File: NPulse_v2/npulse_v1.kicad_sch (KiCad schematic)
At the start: 20 parts, among them J3 Conn_01x04_Pin, J4 USB_B_Micro, SW3 SW_Push, SW4 SW_SPDT, U2 STM32F103C8T6, Y2 16MHz

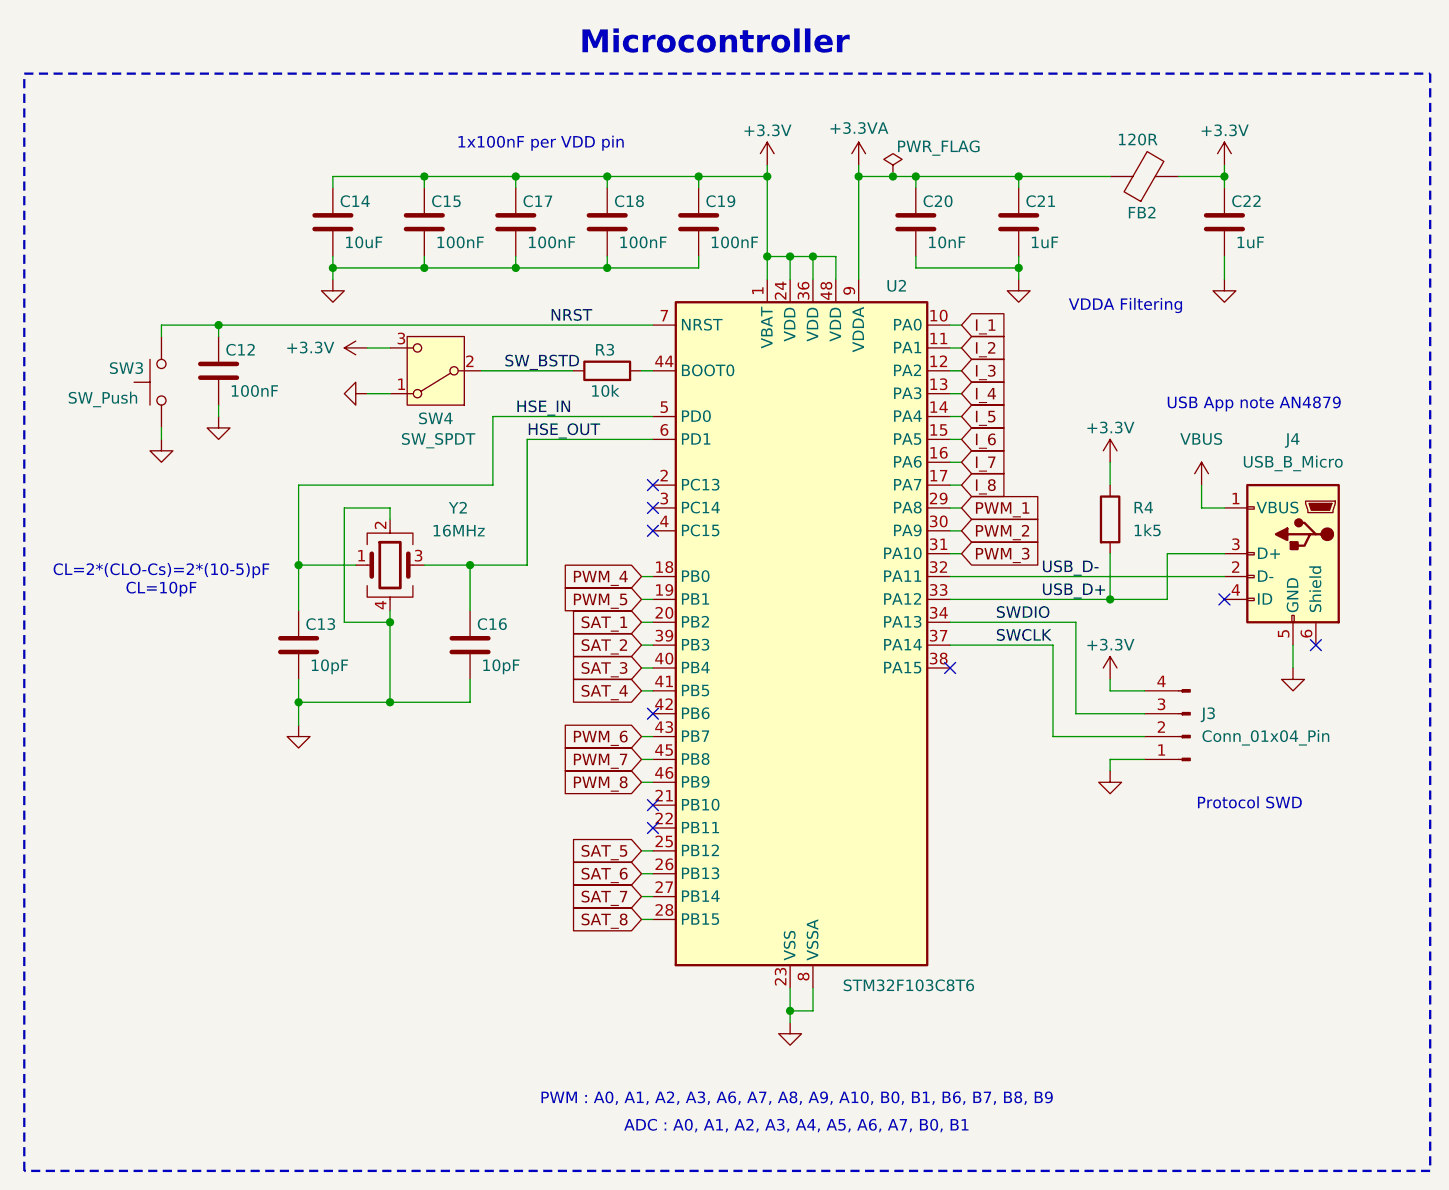
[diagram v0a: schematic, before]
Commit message: Add MCU, FSR, motor drivers, light sensing
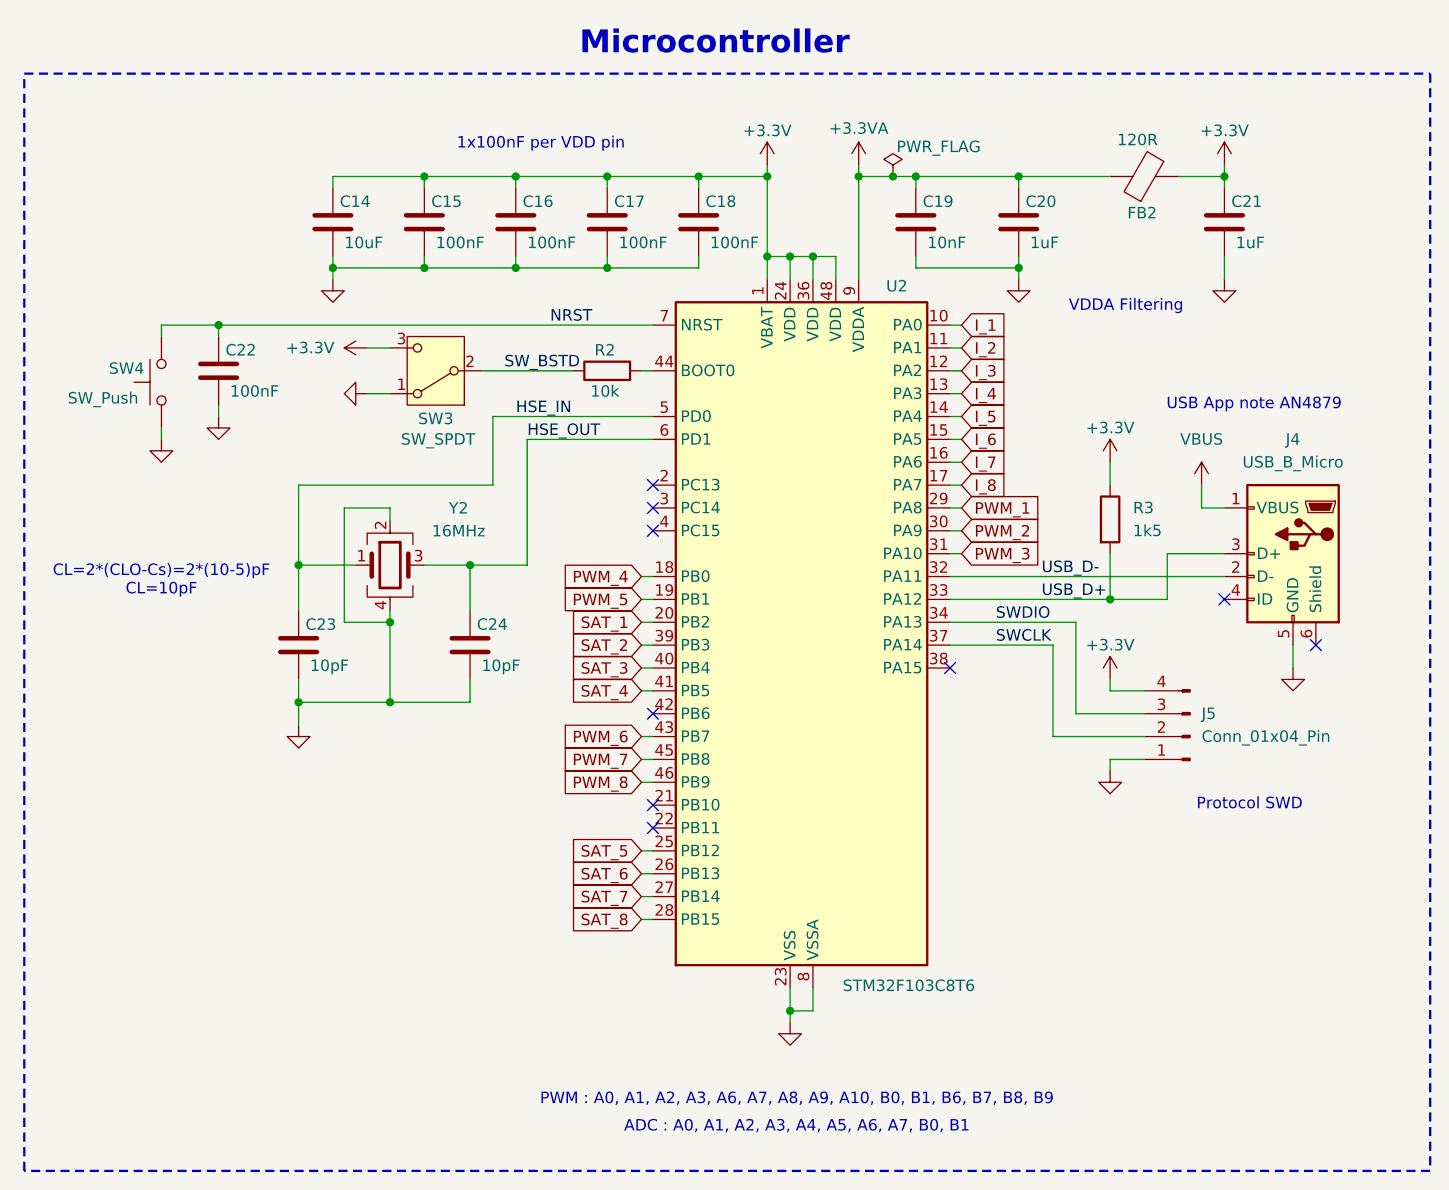
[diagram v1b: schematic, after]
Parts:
- renumbered C17 to C16, C18 to C17, C19 to C18, C20 to C19, C21 to C20, C22 to C21, C12 to C22, C13 to C23, C16 to C24, J3 to J5, R3 to R2, R4 to R3, SW4 to SW3, SW3 to SW4
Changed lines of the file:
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@@
 		(dnp no)
 		(fields_autoplaced yes)
-		(property "Reference" "J3"
+		(property "Reference" "J5"
 			(at 194.31 109.2199 0)
 			(effects
@@
 			(project "NPulse_v2"
 				(path "/cd069ed6-6460-4ce1-aa84-9a9e58749a6a/37ac1c4c-dabe-4c6b-8935-467a17b68a14"
-					(reference "J3")
+					(reference "J5")
 					(unit 1)
 				)
@@
 		(on_board yes)
 		(dnp no)
-		(property "Reference" "C12"
+		(property "Reference" "C22"
 			(at 85.852 68.834 0)
 			(effects
@@
 			(project "NPulse_v2"
 				(path "/cd069ed6-6460-4ce1-aa84-9a9e58749a6a/37ac1c4c-dabe-4c6b-8935-467a17b68a14"
-					(reference "C12")
+					(reference "C22")
 					(unit 1)
 				)
@@
 		(on_board yes)
 		(dnp no)
-		(property "Reference" "#PWR026"
+		(property "Reference" "#PWR017"
 			(at 156.21 52.07 0)
 			(effects
@@
 			(project "NPulse_v2"
 				(path "/cd069ed6-6460-4ce1-aa84-9a9e58749a6a/37ac1c4c-dabe-4c6b-8935-467a17b68a14"
-					(reference "#PWR026")
+					(reference "#PWR017")
 					(unit 1)
 				)
@@
 		(dnp no)
 		(fields_autoplaced yes)
-		(property "Reference" "#PWR019"
+		(property "Reference" "#PWR024"
 			(at 85.09 82.55 0)
 			(effects
@@
 			(project "NPulse_v2"
 				(path "/cd069ed6-6460-4ce1-aa84-9a9e58749a6a/37ac1c4c-dabe-4c6b-8935-467a17b68a14"
-					(reference "#PWR019")
+					(reference "#PWR024")
 					(unit 1)
 				)
@@
 		(on_board yes)
 		(dnp no)
-		(property "Reference" "#PWR028"
+		(property "Reference" "#PWR026"
 			(at 184.15 85.09 0)
 			(effects
@@
 			(project "NPulse_v2"
 				(path "/cd069ed6-6460-4ce1-aa84-9a9e58749a6a/37ac1c4c-dabe-4c6b-8935-467a17b68a14"
-					(reference "#PWR028")
+					(reference "#PWR026")
 					(unit 1)
 				)
@@
 		(dnp no)
 		(fields_autoplaced yes)
-		(property "Reference" "#PWR018"
+		(property "Reference" "#PWR025"
 			(at 78.74 85.09 0)
 			(effects
@@
 			(project "NPulse_v2"
 				(path "/cd069ed6-6460-4ce1-aa84-9a9e58749a6a/37ac1c4c-dabe-4c6b-8935-467a17b68a14"
-					(reference "#PWR018")
+					(reference "#PWR025")
 					(unit 1)
 				)
@@
 		(dnp no)
 		(fields_autoplaced yes)
-		(property "Reference" "R4"
+		(property "Reference" "R3"
 			(at 186.69 86.3599 0)
 			(effects
@@
 			(project "NPulse_v2"
 				(path "/cd069ed6-6460-4ce1-aa84-9a9e58749a6a/37ac1c4c-dabe-4c6b-8935-467a17b68a14"
-					(reference "R4")
+					(reference "R3")
 					(unit 1)
 				)
@@
 		(dnp no)
 		(fields_autoplaced yes)
-		(property "Reference" "#PWR034"
+		(property "Reference" "#PWR028"
 			(at 204.47 110.49 0)
 			(effects
@@
 			(project "NPulse_v2"
 				(path "/cd069ed6-6460-4ce1-aa84-9a9e58749a6a/37ac1c4c-dabe-4c6b-8935-467a17b68a14"
-					(reference "#PWR034")
+					(reference "#PWR028")
 					(unit 1)
 				)
@@
 		(on_board yes)
 		(dnp no)
-		(property "Reference" "C16"
+		(property "Reference" "C24"
 			(at 113.792 99.314 0)
 			(effects
@@
 			(project "NPulse_v2"
 				(path "/cd069ed6-6460-4ce1-aa84-9a9e58749a6a/37ac1c4c-dabe-4c6b-8935-467a17b68a14"
-					(reference "C16")
+					(reference "C24")
 					(unit 1)
 				)
@@
 		(dnp no)
 		(fields_autoplaced yes)
-		(property "Reference" "#PWR021"
+		(property "Reference" "#PWR019"
 			(at 97.79 67.31 0)
 			(effects
@@
 			(project "NPulse_v2"
 				(path "/cd069ed6-6460-4ce1-aa84-9a9e58749a6a/37ac1c4c-dabe-4c6b-8935-467a17b68a14"
-					(reference "#PWR021")
+					(reference "#PWR019")
 					(unit 1)
 				)
@@
 		(on_board yes)
 		(dnp no)
-		(property "Reference" "SW3"
+		(property "Reference" "SW4"
 			(at 72.898 70.866 90)
 			(effects
@@
 			(project "NPulse_v2"
 				(path "/cd069ed6-6460-4ce1-aa84-9a9e58749a6a/37ac1c4c-dabe-4c6b-8935-467a17b68a14"
-					(reference "SW3")
+					(reference "SW4")
 					(unit 1)
 				)
@@
 		(on_board yes)
 		(dnp no)
-		(property "Reference" "#PWR024"
+		(property "Reference" "#PWR016"
 			(at 146.05 52.07 0)
 			(effects
@@
 			(project "NPulse_v2"
 				(path "/cd069ed6-6460-4ce1-aa84-9a9e58749a6a/37ac1c4c-dabe-4c6b-8935-467a17b68a14"
-					(reference "#PWR024")
+					(reference "#PWR016")
 					(unit 1)
 				)
@@
 		(on_board yes)
 		(dnp no)
-		(property "Reference" "C13"
+		(property "Reference" "C23"
 			(at 94.742 99.314 0)
 			(effects
@@
 			(project "NPulse_v2"
 				(path "/cd069ed6-6460-4ce1-aa84-9a9e58749a6a/37ac1c4c-dabe-4c6b-8935-467a17b68a14"
-					(reference "C13")
+					(reference "C23")
 					(unit 1)
 				)
@@
 		(on_board yes)
 		(dnp no)
-		(property "Reference" "#PWR032"
+		(property "Reference" "#PWR018"
 			(at 196.85 52.07 0)
 			(effects
@@
 			(project "NPulse_v2"
 				(path "/cd069ed6-6460-4ce1-aa84-9a9e58749a6a/37ac1c4c-dabe-4c6b-8935-467a17b68a14"
-					(reference "#PWR032")
+					(reference "#PWR018")
 					(unit 1)
 				)
@@
 		(dnp no)
 		(fields_autoplaced yes)
-		(property "Reference" "#PWR027"
+		(property "Reference" "#PWR020"
 			(at 173.99 67.31 0)
 			(effects
@@
 			(project "NPulse_v2"
 				(path "/cd069ed6-6460-4ce1-aa84-9a9e58749a6a/37ac1c4c-dabe-4c6b-8935-467a17b68a14"
-					(reference "#PWR027")
+					(reference "#PWR020")
 					(unit 1)
 				)
@@
 		(on_board yes)
 		(dnp no)
-		(property "Reference" "SW4"
+		(property "Reference" "SW3"
 			(at 109.22 76.454 0)
 			(effects
@@
 			(project "NPulse_v2"
 				(path "/cd069ed6-6460-4ce1-aa84-9a9e58749a6a/37ac1c4c-dabe-4c6b-8935-467a17b68a14"
-					(reference "SW4")
+					(reference "SW3")
 					(unit 1)
 				)
@@
 		(on_board yes)
 		(dnp no)
-		(property "Reference" "C17"
+		(property "Reference" "C16"
 			(at 118.872 52.324 0)
 			(effects
@@
 			(project "NPulse_v2"
 				(path "/cd069ed6-6460-4ce1-aa84-9a9e58749a6a/37ac1c4c-dabe-4c6b-8935-467a17b68a14"
-					(reference "C17")
+					(reference "C16")
 					(unit 1)
 				)
@@
 		(dnp no)
 		(fields_autoplaced yes)
-		(property "Reference" "#PWR033"
+		(property "Reference" "#PWR021"
 			(at 196.85 67.31 0)
 			(effects
@@
 			(project "NPulse_v2"
 				(path "/cd069ed6-6460-4ce1-aa84-9a9e58749a6a/37ac1c4c-dabe-4c6b-8935-467a17b68a14"
-					(reference "#PWR033")
+					(reference "#PWR021")
 					(unit 1)
 				)
@@
 		(on_board yes)
 		(dnp no)
-		(property "Reference" "C18"
+		(property "Reference" "C17"
 			(at 129.032 52.324 0)
 			(effects
@@
 			(project "NPulse_v2"
 				(path "/cd069ed6-6460-4ce1-aa84-9a9e58749a6a/37ac1c4c-dabe-4c6b-8935-467a17b68a14"
-					(reference "C18")
+					(reference "C17")
 					(unit 1)
 				)
@@
 		(on_board yes)
 		(dnp no)
-		(property "Reference" "C20"
+		(property "Reference" "C19"
 			(at 163.322 52.324 0)
 			(effects
@@
 			(project "NPulse_v2"
 				(path "/cd069ed6-6460-4ce1-aa84-9a9e58749a6a/37ac1c4c-dabe-4c6b-8935-467a17b68a14"
-					(reference "C20")
+					(reference "C19")
 					(unit 1)
 				)
@@
 		(on_board yes)
 		(dnp no)
-		(property "Reference" "R3"
+		(property "Reference" "R2"
 			(at 128.016 68.834 90)
 			(effects
@@
 			(project "NPulse_v2"
 				(path "/cd069ed6-6460-4ce1-aa84-9a9e58749a6a/37ac1c4c-dabe-4c6b-8935-467a17b68a14"
-					(reference "R3")
+					(reference "R2")
 					(unit 1)
 				)
@@
 		(on_board yes)
 		(dnp no)
-		(property "Reference" "C22"
+		(property "Reference" "C21"
 			(at 197.612 52.324 0)
 			(effects
@@
 			(project "NPulse_v2"
 				(path "/cd069ed6-6460-4ce1-aa84-9a9e58749a6a/37ac1c4c-dabe-4c6b-8935-467a17b68a14"
-					(reference "C22")
+					(reference "C21")
 					(unit 1)
 				)
@@
 		(dnp no)
 		(fields_autoplaced yes)
-		(property "Reference" "#PWR020"
+		(property "Reference" "#PWR030"
 			(at 93.98 116.84 0)
 			(effects
@@
 			(project "NPulse_v2"
 				(path "/cd069ed6-6460-4ce1-aa84-9a9e58749a6a/37ac1c4c-dabe-4c6b-8935-467a17b68a14"
-					(reference "#PWR020")
+					(reference "#PWR030")
 					(unit 1)
 				)
@@
 		(on_board yes)
 		(dnp no)
-		(property "Reference" "C21"
+		(property "Reference" "C20"
 			(at 174.752 52.324 0)
 			(effects
@@
 			(project "NPulse_v2"
 				(path "/cd069ed6-6460-4ce1-aa84-9a9e58749a6a/37ac1c4c-dabe-4c6b-8935-467a17b68a14"
-					(reference "C21")
+					(reference "C20")
 					(unit 1)
 				)
@@
 		(dnp no)
 		(fields_autoplaced yes)
-		(property "Reference" "#PWR030"
+		(property "Reference" "#PWR031"
 			(at 184.15 121.92 0)
 			(effects
@@
 			(project "NPulse_v2"
 				(path "/cd069ed6-6460-4ce1-aa84-9a9e58749a6a/37ac1c4c-dabe-4c6b-8935-467a17b68a14"
-					(reference "#PWR030")
+					(reference "#PWR031")
 					(unit 1)
 				)
@@
 		(dnp no)
 		(fields_autoplaced yes)
-		(property "Reference" "#PWR031"
+		(property "Reference" "#PWR027"
 			(at 194.31 87.63 0)
 			(effects
@@
 			(project "NPulse_v2"
 				(path "/cd069ed6-6460-4ce1-aa84-9a9e58749a6a/37ac1c4c-dabe-4c6b-8935-467a17b68a14"
-					(reference "#PWR031")
+					(reference "#PWR027")
 					(unit 1)
 				)
@@
 		(on_board yes)
 		(dnp no)
-		(property "Reference" "C19"
+		(property "Reference" "C18"
 			(at 139.192 52.324 0)
 			(effects
@@
 			(project "NPulse_v2"
 				(path "/cd069ed6-6460-4ce1-aa84-9a9e58749a6a/37ac1c4c-dabe-4c6b-8935-467a17b68a14"
-					(reference "C19")
+					(reference "C18")
 					(unit 1)
 				)
@@
 		(dnp no)
 		(fields_autoplaced yes)
-		(property "Reference" "#PWR025"
+		(property "Reference" "#PWR032"
 			(at 148.59 149.86 0)
 			(effects
@@
 			(project "NPulse_v2"
 				(path "/cd069ed6-6460-4ce1-aa84-9a9e58749a6a/37ac1c4c-dabe-4c6b-8935-467a17b68a14"
-					(reference "#PWR025")
-					(unit 1)
-				)
+					(reference "#PWR032")
+					(unit 1)
+				)
